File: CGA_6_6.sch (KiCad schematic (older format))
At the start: 43 parts, among them J1 VIDEO JACK, J2 RGBI Output, P1 1X4 BERG, P2 1X6 BERG, P5 Bus_ISA_8bit, U13 74LS08, U14 74LS32, U20 74LS04, U26 74S04, U41 74LS08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

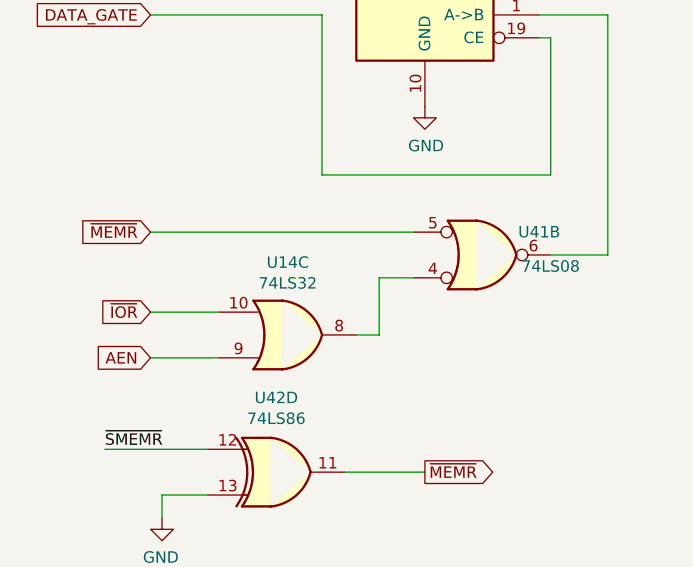
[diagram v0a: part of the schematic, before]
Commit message: Fix IC type
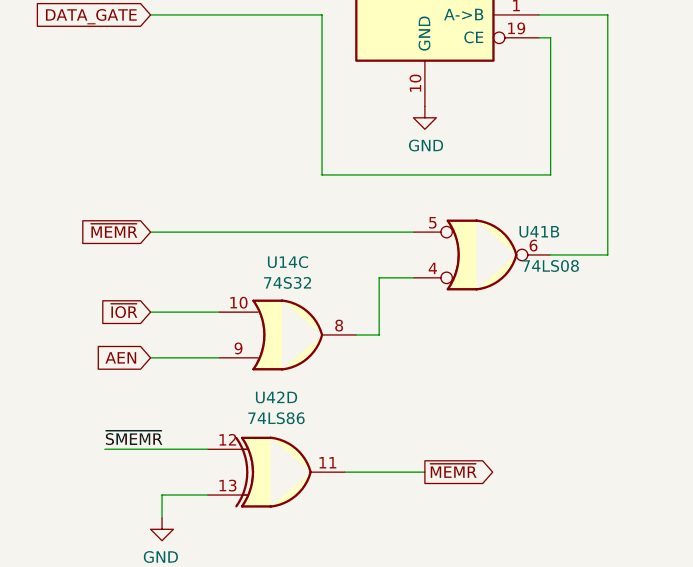
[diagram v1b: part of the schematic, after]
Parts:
- U14: value 74LS32 -> 74S32
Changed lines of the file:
@@
 AR Path="/60463D9E/64CA00B2" Ref="U14"  Part="3"
 F 0 "U14" H 2000 3283 50  0000 C CNN
-F 1 "74LS32" H 2000 3374 50  0000 C CNN
+F 1 "74S32" H 2000 3374 50  0000 C CNN
 F 2 "Package_DIP:DIP-14_W7.62mm_LongPads" H 2000 3600 50  0001 C CNN
 F 3 "http://www.ti.com/lit/gpn/sn74LS32" H 2000 3600 50  0001 C CNN
